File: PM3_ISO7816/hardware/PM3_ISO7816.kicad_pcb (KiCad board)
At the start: 2 copper layers, 17 x 24.5 mm, 10 parts, among them J1 Smartcard Slot, J2 Conn_01x05, J3 Conn_01x05, U1 N76E003AT20

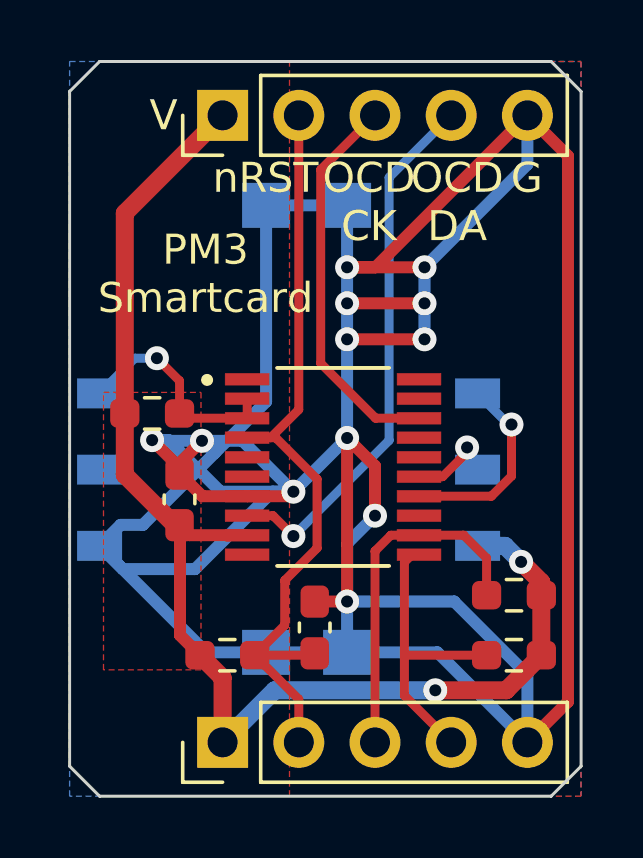
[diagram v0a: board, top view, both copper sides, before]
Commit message: Smartcard: Misc work on PCB
Swap VCC pin and GND pin to match the pin order of Nu-Link
Change the footprint of sim card slot for hand soldering
Add test points
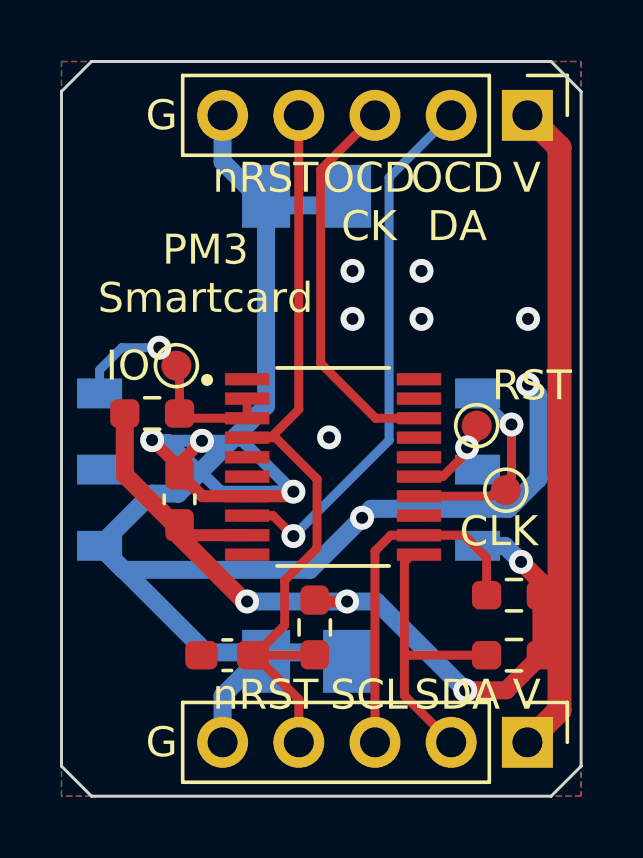
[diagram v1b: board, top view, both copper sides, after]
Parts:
- added TP1: TestPoint, TestPoint:TestPoint_Pad_D1.0mm, F.Cu at (72.0, 56.1)
- added TP2: TestPoint, TestPoint:TestPoint_Pad_D1.0mm, F.Cu at (73.0, 58.2)
- added TP3: TestPoint, TestPoint:TestPoint_Pad_D1.0mm, F.Cu at (62.0, 54.1)
- moved J2 10.2 mm to (73.7, 66.6), turned to -90 degrees
- moved J3 10.2 mm to (73.7, 45.7), turned to -90 degrees
- moved C2 3.06 mm to (63.7, 63.7), turned to 180 degrees
- moved R3 3.06 mm to (66.6, 62.8), turned to -90 degrees
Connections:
- J2 pad 2: /nRST -> /SDA
- J2 pad 4: /SDA -> /nRST
- J3 pad 2: /nRST -> /OCDDA
- J3 pad 4: /OCDDA -> /nRST
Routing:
- net GND: track 140.9 -> 72.5 mm, vias 12 -> 11
- net VCC: track 43.0 -> 49.4 mm, vias 2 -> 4
- net /slot_IO: track 7.52 -> 8.52 mm
- net /slot_RST: track 2.98 -> 3.84 mm
- removed copper zone on F.Cu, net VCC
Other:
- board size 17 x 24.5 mm -> 17.3 x 24.5 mm
- board text added: "CLK"
- board text added: "I O"
- board text added: "IO"
- board text added: "RST"
